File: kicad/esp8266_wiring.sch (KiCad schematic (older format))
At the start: 20 parts, among them J1 Conn_02x08_Odd_Even, J8 UART, Q4 DMG2301L, U4 ESP-WROOM-02, U5 TPL5110

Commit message: Libraries cleanup
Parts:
- gave numbers to parts that had none: 2
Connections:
- net labels added: BATT_SENS
- wire segments 34 -> 36
- no-connect marks 1 -> 0
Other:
- note added: "DRV is \nACTIVE LOW"
- note removed: "DRV is ACTIVE LOW"

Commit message: Charger initial wiring complete
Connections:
- net labels added: BATT_GAUGE_SHDN
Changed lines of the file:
@@
 Text Label 7250 5200 0    50   ~ 0
 ALL_EN
+Text GLabel 4900 3250 0    50   Input ~ 0
+BATT_GAUGE_SHDN
 $EndSCHEMATC

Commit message: Schematics cleanup
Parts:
- removed J1: Conn_02x08_Odd_Even, Connector_PinHeader_2.54mm:PinHeader_2x08_P2.54mm_Vertical, symbol Connector_Generic:Conn_02x08_Odd_Even
- removed J8: UART, Connector_PinHeader_2.54mm:PinHeader_1x06_P2.54mm_Vertical, symbol Connector_Generic:Conn_01x06
- removed R11: 10K, Resistor_SMD:R_0805_2012Metric, symbol Device:R
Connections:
- net labels added: BOOT_MODE, CHIP_RESET, SYS_EN, SYS_EN_DRV, UART_RXD, UART_TXD
- net labels removed: BATT_SENS, GPIO12, USB_RXD, USB_TXD, VDD
- wire segments 36 -> 54
- no-connect marks 0 -> 1
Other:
- note added: "Config"
- note added: "ESP8266"
- note added: "System Enable Driver block\n(Active High)"
- note added: "System Sleep Timer"
- note removed: "Config and pull"
- note removed: "Host Wake Up (active high)"
- note removed: "I2C Pull Up"
- moved on the sheet: C10, C6, C8, C9, Q2, Q4, R10, R12, R13, R17, R2, R3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

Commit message: Comitting yesterday's leftovers
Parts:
- removed C9: 0.1μF, Capacitor_SMD:C_1206_3216Metric, symbol Device:C
- removed Q2: DTC113Z, symbol Transistor_BJT:DTC113Z
- removed Q4: DMG2301L, Package_TO_SOT_SMD:SOT-23, symbol Transistor_FET:DMG2301L
- added C3: 0.1μF, Capacitor_SMD:C_1206_3216Metric, symbol Device:C
- added D2, D3: LED, LED_SMD:LED_0603_1608Metric, symbol Device:LED
- added R10: 4.7K, symbol Device:R
- added R2, R3: 2K, Resistor_SMD:R_0805_2012Metric, symbol Device:R
- added R9: 10K, symbol Device:R
- added SW1: SW_Wakeup, symbol Switch:SW_Push
- added SW2: SW_Reset, symbol Switch:SW_Push
- added U2: SSM6L40TU, Parts:SSM6L40TU, symbol Parts:SSM6L40TU
- renumbered C10 to C1, C6 to C2, C8 to C4, R10 to R1, R17 to R11, R2 to R12, R6 to R13, R13 to R4, R12 to R5, R3 to R6, R9 to R8, U4 to U1, U5 to U3
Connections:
- net GPIO0 is gone; now on net BOOT_MODE: R4.2
- net WAKE_UP is gone; now on net HOST_WAKE_UP: R7.2
- net +3V3: now also R3.2, R9.2
- net CHIP_RESET: now also SW2.1
- net GND: now also C3.1, D2.1 (K), D3.1 (K), R10.2
- net HOST_WAKE_UP: now also SW1.1, U2.2 (G1)
- net SYS_EN: now also C3.2, R2.2, U2.3 (D2)
- net SYS_EN_DRV: now also U2.5 (G2)
- net at R11.2: now also U2.4 (S2), U2.6 (D1)
- net TPL_MDRV: now reaches R12.1, R13.1, U3.3 (DELAY/M_DRV)
- net TPL_MDRV: now also U2.1 (S1)
- net GPIO13 renamed nCH_PGOOD
- new net: D3.2 (A), R3.1
- new net: D2.2 (A), R2.1
- new net: R10.1, SW2.2
- new net: R9.1, SW1.2
- no-connect marks 1 -> 2
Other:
- note added: "ACTIVE LOW"
- note added: "Does SYS_EN provide enough \npower to power this LED?"
- note added: "Manual Switches"
- note added: "Todo: Figure out how to kick the timer to enable \nthe system for one round. The system will sleep \nagain if it decides it doesn't need to run."
- note removed: "DRV is \nACTIVE LOW"
- note removed: "System Enable Driver block\n(Active High)"
- moved on the sheet: C1, C2, R1, R11, R4, R5, R6, R7, R8, U1

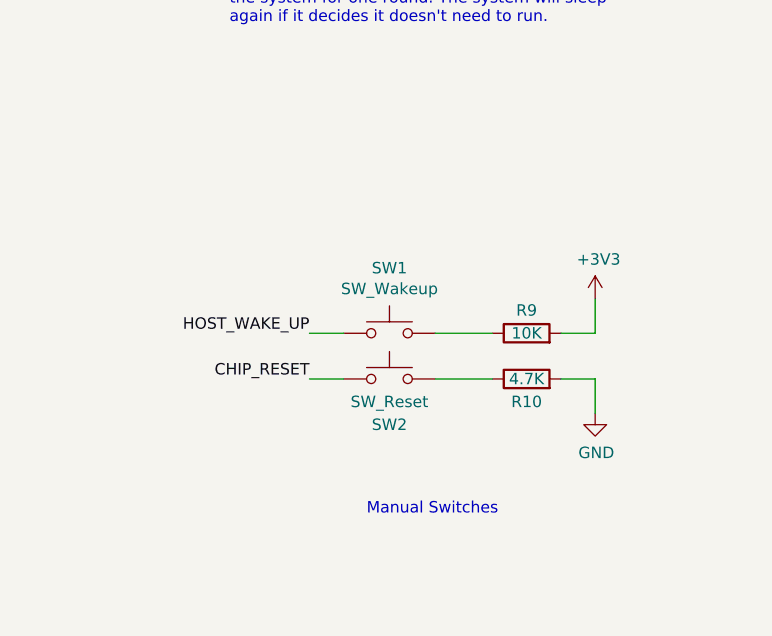
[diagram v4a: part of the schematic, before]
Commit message: Relabeled and completed ERC
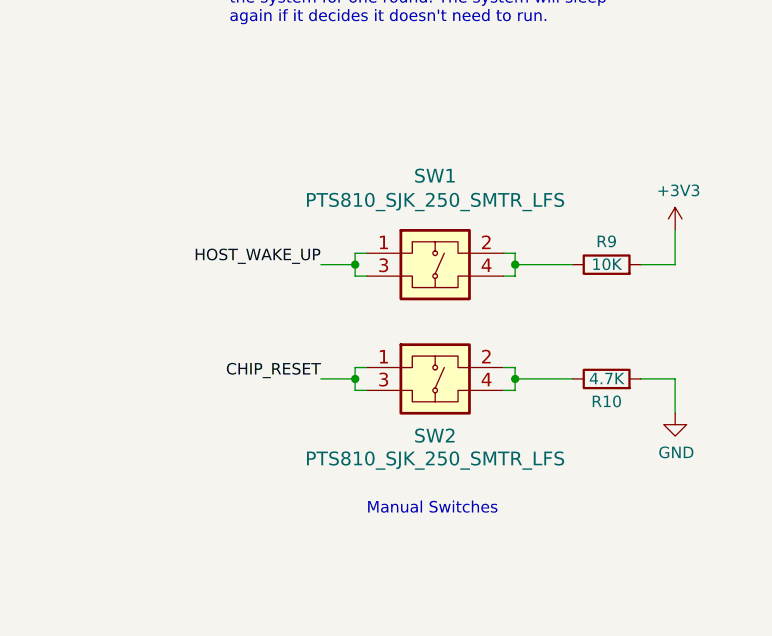
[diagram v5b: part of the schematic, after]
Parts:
- removed SW1: SW_Wakeup, symbol Switch:SW_Push
- removed SW2: SW_Reset, symbol Switch:SW_Push
- added SW1, SW2: PTS810_SJK_250_SMTR_LFS, Parts:PTS810 SJK 250 SMTR LFS, symbol Parts:PTS810_SJK_250_SMTR_LFS
- R10, R9: footprint (none) -> Resistor_SMD:R_0805_2012Metric
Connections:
- net CHIP_RESET: now also SW2.1, SW2.3
- net HOST_WAKE_UP: now also SW1.1, SW1.3
- net at R10.1: now also SW2.2, SW2.4
- net at R9.1: now also SW1.2, SW1.4
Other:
- moved on the sheet: R10, R9
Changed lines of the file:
@@
 Does SYS_EN provide enough \npower to power this LED?
-$Comp
-L Switch:SW_Push SW2
-U 1 1 610C680A
-P 8950 4850
-F 0 "SW2" H 8950 4650 50  0000 C CNN
-F 1 "SW_Reset" H 8950 4750 50  0000 C CNN
-F 2 "" H 8950 5050 50  0001 C CNN
-F 3 "~" H 8950 5050 50  0001 C CNN
-	1    8950 4850
-	1    0    0    -1
-$EndComp
-$Comp
-L Switch:SW_Push SW1
-U 1 1 610C7B67
-P 8950 4650
-F 0 "SW1" H 8950 4935 50  0000 C CNN
-F 1 "SW_Wakeup" H 8950 4844 50  0000 C CNN
-F 2 "" H 8950 4850 50  0001 C CNN
-F 3 "~" H 8950 4850 50  0001 C CNN
-	1    8950 4650
-	1    0    0    -1
-$EndComp
 $Comp
 L Device:R R9
 U 1 1 610C84A2
-P 9550 4650
-F 0 "R9" V 9650 4650 50  0000 C CNN
-F 1 "10K" V 9550 4650 50  0000 C CNN
-F 2 "" V 9480 4650 50  0001 C CNN
-F 3 "~" H 9550 4650 50  0001 C CNN
-	1    9550 4650
+P 9900 4350
+F 0 "R9" V 10000 4350 50  0000 C CNN
+F 1 "10K" V 9900 4350 50  0000 C CNN
+F 2 "Resistor_SMD:R_0805_2012Metric" V 9830 4350 50  0001 C CNN
+F 3 "~" H 9900 4350 50  0001 C CNN
+	1    9900 4350
 	0    -1   -1   0
 $EndComp
 Wire Wire Line
-	9400 4650 9150 4650
+	9750 4350 9500 4350
 $Comp
 L power:+3V3 #PWR021
 U 1 1 610CA54C
-P 9850 4500
-F 0 "#PWR021" H 9850 4350 50  0001 C CNN
-F 1 "+3V3" H 9865 4673 50  0000 C CNN
-F 2 "" H 9850 4500 50  0001 C CNN
-F 3 "" H 9850 4500 50  0001 C CNN
-	1    9850 4500
+P 10200 4200
+F 0 "#PWR021" H 10200 4050 50  0001 C CNN
+F 1 "+3V3" H 10215 4373 50  0000 C CNN
+F 2 "" H 10200 4200 50  0001 C CNN
+F 3 "" H 10200 4200 50  0001 C CNN
+	1    10200 4200
 	1    0    0    -1
 $EndComp
-Text Label 8600 4650 2    50   ~ 0
+Text Label 8650 4350 2    50   ~ 0
 HOST_WAKE_UP
 $Comp
 L power:GND #PWR025
 U 1 1 610D24DB
-P 9850 5000
-F 0 "#PWR025" H 9850 4750 50  0001 C CNN
-F 1 "GND" H 9855 4827 50  0000 C CNN
-F 2 "" H 9850 5000 50  0001 C CNN
-F 3 "" H 9850 5000 50  0001 C CNN
-	1    9850 5000
+P 10200 5000
+F 0 "#PWR025" H 10200 4750 50  0001 C CNN
+F 1 "GND" H 10205 4827 50  0000 C CNN
+F 2 "" H 10200 5000 50  0001 C CNN
+F 3 "" H 10200 5000 50  0001 C CNN
+	1    10200 5000
 	1    0    0    -1
 $EndComp
@@
 L Device:R R10
 U 1 1 610D3AFC
-P 9550 4850
-F 0 "R10" V 9450 4850 50  0000 C CNN
-F 1 "4.7K" V 9550 4850 50  0000 C CNN
-F 2 "" V 9480 4850 50  0001 C CNN
-F 3 "~" H 9550 4850 50  0001 C CNN
-	1    9550 4850
+P 9900 4850
+F 0 "R10" V 9800 4850 50  0000 C CNN
+F 1 "4.7K" V 9900 4850 50  0000 C CNN
+F 2 "Resistor_SMD:R_0805_2012Metric" V 9830 4850 50  0001 C CNN
+F 3 "~" H 9900 4850 50  0001 C CNN
+	1    9900 4850
 	0    -1   -1   0
 $EndComp
 Wire Wire Line
-	9400 4850 9150 4850
+	9750 4850 9500 4850
 Wire Wire Line
-	9850 4850 9850 5000
+	10200 4850 10200 5000
 Wire Wire Line
-	9700 4850 9850 4850
+	10050 4850 10200 4850
 Wire Wire Line
-	9850 4650 9700 4650
+	10200 4350 10050 4350
 Wire Wire Line
-	8750 4650 8600 4650
-Text Label 8600 4850 2    50   ~ 0
+	8800 4350 8650 4350
+Text Label 8650 4850 2    50   ~ 0
 CHIP_RESET
 Wire Wire Line
-	8600 4850 8750 4850
+	8650 4850 8800 4850
 Wire Wire Line
-	9850 4500 9850 4650
+	10200 4200 10200 4350
 Text HLabel 8950 2900 2    50   Input ~ 0
 nCH_PGOOD
@@
 Text Label 8950 2900 2    50   ~ 0
 nCH_PGOOD
+Wire Wire Line
+	9450 4300 9500 4300
+Wire Wire Line
+	9500 4300 9500 4350
+Wire Wire Line
+	9500 4400 9450 4400
+Connection ~ 9500 4350
+Wire Wire Line
+	9500 4350 9500 4400
+Wire Wire Line
+	9450 4800 9500 4800
+Wire Wire Line
+	9500 4800 9500 4850
+Wire Wire Line
+	9500 4900 9450 4900
+Connection ~ 9500 4850
+Wire Wire Line
+	9500 4850 9500 4900
+Wire Wire Line
+	8850 4900 8800 4900
+Wire Wire Line
+	8800 4900 8800 4850
+Wire Wire Line
+	8800 4800 8850 4800
+Connection ~ 8800 4850
+Wire Wire Line
+	8800 4850 8800 4800
+Wire Wire Line
+	8850 4400 8800 4400
+Wire Wire Line
+	8800 4400 8800 4350
+Wire Wire Line
+	8800 4300 8850 4300
+Connection ~ 8800 4350
+Wire Wire Line
+	8800 4350 8800 4300
+$Comp
+L Parts:PTS810_SJK_250_SMTR_LFS SW1
+U 1 1 6123F9FD
+P 9150 4350
+F 0 "SW1" H 9150 4737 60  0000 C CNN
+F 1 "PTS810_SJK_250_SMTR_LFS" H 9150 4631 60  0000 C CNN
+F 2 "Parts:PTS810 SJK 250 SMTR LFS" H 9150 4640 60  0001 C CNN
+F 3 "" H 8350 4400 60  0000 C CNN
+	1    9150 4350
+	1    0    0    -1
+$EndComp
+$Comp
+L Parts:PTS810_SJK_250_SMTR_LFS SW2
+U 1 1 61240932
+P 9150 4850
+F 0 "SW2" H 9150 4600 60  0000 C CNN
+F 1 "PTS810_SJK_250_SMTR_LFS" H 9150 4500 60  0000 C CNN
+F 2 "Parts:PTS810 SJK 250 SMTR LFS" H 9150 5140 60  0001 C CNN
+F 3 "" H 8350 4900 60  0000 C CNN
+	1    9150 4850
+	1    0    0    -1
+$EndComp
 $EndSCHEMATC

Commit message: Mapped footprints, PCB in progress
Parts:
- SW1, SW2: footprint Parts:PTS810 SJK 250 SMTR LFS -> Parts:PTS810SJK250SMTRLFS
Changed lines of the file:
@@
 F 0 "SW1" H 9150 4737 60  0000 C CNN
 F 1 "PTS810_SJK_250_SMTR_LFS" H 9150 4631 60  0000 C CNN
-F 2 "Parts:PTS810 SJK 250 SMTR LFS" H 9150 4640 60  0001 C CNN
+F 2 "Parts:PTS810SJK250SMTRLFS" H 9150 4640 60  0001 C CNN
 F 3 "" H 8350 4400 60  0000 C CNN
 	1    9150 4350
@@
 F 0 "SW2" H 9150 4600 60  0000 C CNN
 F 1 "PTS810_SJK_250_SMTR_LFS" H 9150 4500 60  0000 C CNN
-F 2 "Parts:PTS810 SJK 250 SMTR LFS" H 9150 5140 60  0001 C CNN
+F 2 "Parts:PTS810SJK250SMTRLFS" H 9150 5140 60  0001 C CNN
 F 3 "" H 8350 4900 60  0000 C CNN
 	1    9150 4850
